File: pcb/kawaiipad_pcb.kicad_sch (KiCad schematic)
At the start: 21 parts, among them SW1 SW_Push_45deg, SW2 SW_Push_45deg, SW3 SW_Push_45deg, SW4 SW_Push_45deg, SW5 SW_Push_45deg, SW6 SW_Push_45deg, SW7 SW_Push_45deg, SW8 SW_Push_45deg, SW9 SW_Push_45deg, U1 XIAO-RP2040-DIP

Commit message: Update kawaiipad_pcb.kicad_sch
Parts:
- removed D1, D2: SK6812MINI, LED_SMD:LED_SK6812MINI_PLCC4_3.5x3.5mm_P1.75mm, symbol LED:SK6812MINI
- removed D10, D11: D, DiodeLibrary:Diode-Hybrid-Dual, symbol Device:D
- added D1, D2: D, symbol Device:D
- added D10, D11, D12, D13, D15, D16, D17, D18, D19: SK6812MINI, LED_SMD:LED_SK6812MINI_PLCC4_3.5x3.5mm_P1.75mm, symbol LED:SK6812MINI
- D3, D4, D5, D6, D7, D8, D9: footprint DiodeLibrary:Diode-Hybrid-Dual -> (none)
- SW1, SW2, SW3, SW4, SW5, SW6, SW7, SW8, SW9: footprint Button_Switch_Keyboard:SW_Cherry_MX_1.00u_PCB -> (none)
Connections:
- net +5V: now also D10.4 (VDD), D11.4 (VDD), D12.4 (VDD), D13.4 (VDD), D15.4 (VDD), D16.4 (VDD), D17.4 (VDD), D18.4 (VDD), D19.4 (VDD)
- net GND: now also D10.2 (VSS), D11.2 (VSS), D12.2 (VSS), D13.2 (VSS), D15.2 (VSS), D16.2 (VSS), D17.2 (VSS), D18.2 (VSS), D19.2 (VSS)
- net LED: now also D10.3 (DIN)
- net Row 0: now also D1.1 (K), D2.1 (K); no longer D4.1 (K), D5.1 (K)
- net Row 1: now also D4.1 (K), D5.1 (K); no longer D7.1 (K), D8.1 (K)
- net Row 2: now also D7.1 (K), D8.1 (K)
- net at SW8.2: now also D8.2 (A)
- net at D9.2 (A): now also SW9.2; no longer SW7.2
- net at SW6.2: now also D6.2 (A); no longer D8.2 (A)
- net at SW5.2: now also D5.2 (A); no longer D7.2 (A)
- net at SW4.2: now also D4.2 (A); no longer D6.2 (A)
- net at SW1.2: now also D1.2 (A); no longer D3.2 (A)
- net at SW3.2: now also D3.2 (A); no longer D5.2 (A)
- net at SW2.2: now also D2.2 (A); no longer D4.2 (A)
- new net: D10.1 (DOUT), D11.3 (DIN)
- new net: D11.1 (DOUT), D12.3 (DIN)
- new net: D16.1 (DOUT), D17.3 (DIN)
- new net: D15.1 (DOUT), D16.3 (DIN)
- new net: D7.2 (A), SW7.2
- new net: D12.1 (DOUT), D13.3 (DIN)
- new net: D13.1 (DOUT), D15.3 (DIN)
- new net: D18.1 (DOUT), D19.3 (DIN)
- new net: D17.1 (DOUT), D18.3 (DIN)
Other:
- note added: "RGB LEDs"
- note added: "RP2040 MCU"
- note added: "SWITCHES"
- title: (none) -> KawaiiPad
- moved on the sheet: U1

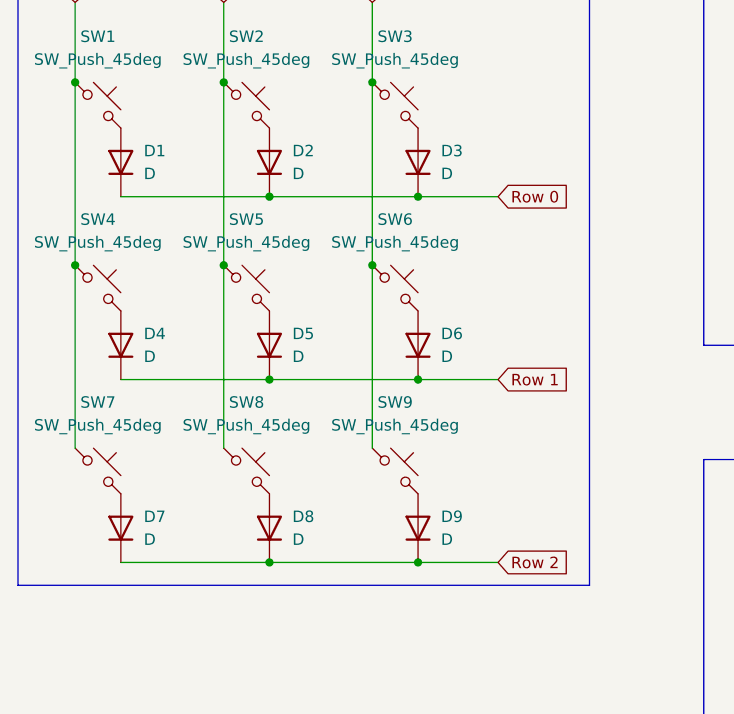
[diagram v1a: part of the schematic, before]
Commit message: Add Diode 1N418, remove accidental extra LEDs, assign footprints
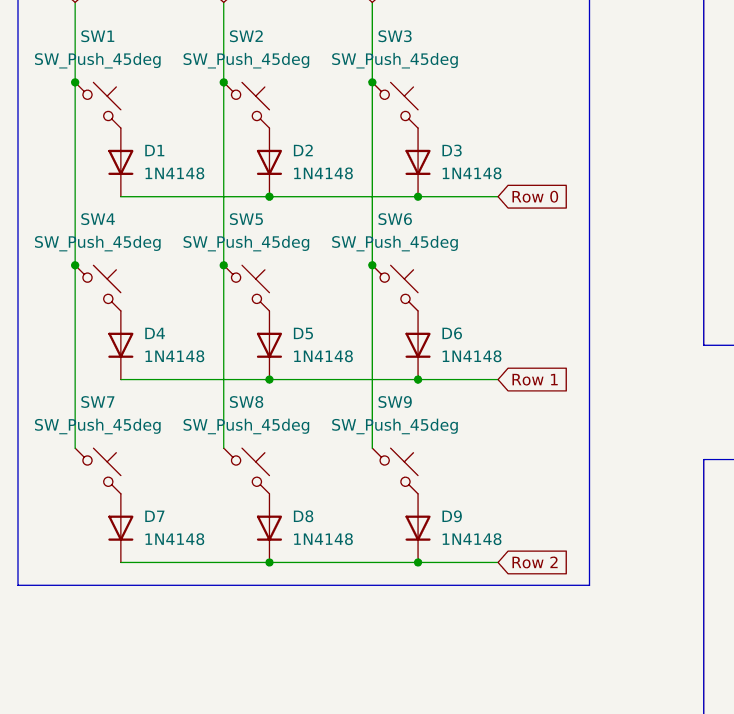
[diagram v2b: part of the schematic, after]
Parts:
- removed D1, D2, D3, D4, D5, D6, D7, D8, D9: D, symbol Device:D
- added D1, D2, D3, D4, D5, D6, D7, D8, D9: 1N4148, DiodeLibrary:DIODE-1N4148, symbol Diode:1N4148
- SW1, SW2, SW3, SW4, SW5, SW6, SW7, SW8, SW9: footprint (none) -> Button_Switch_Keyboard:SW_Cherry_MX_1.00u_PCB
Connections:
- net Row 0: now also D1.1 (K), D2.1 (K), D3.1 (K)
- net Row 1: now also D4.1 (K), D5.1 (K), D6.1 (K)
- net Row 2: now also D7.1 (K), D8.1 (K), D9.1 (K)
- net at SW9.2: now also D9.2 (A)
- net at SW4.2: now also D4.2 (A)
- net at SW5.2: now also D5.2 (A)
- net at SW1.2: now also D1.2 (A)
- net at SW7.2: now also D7.2 (A)
- net at SW6.2: now also D6.2 (A)
- net at SW2.2: now also D2.2 (A)
- net at SW8.2: now also D8.2 (A)
- net at SW3.2: now also D3.2 (A)

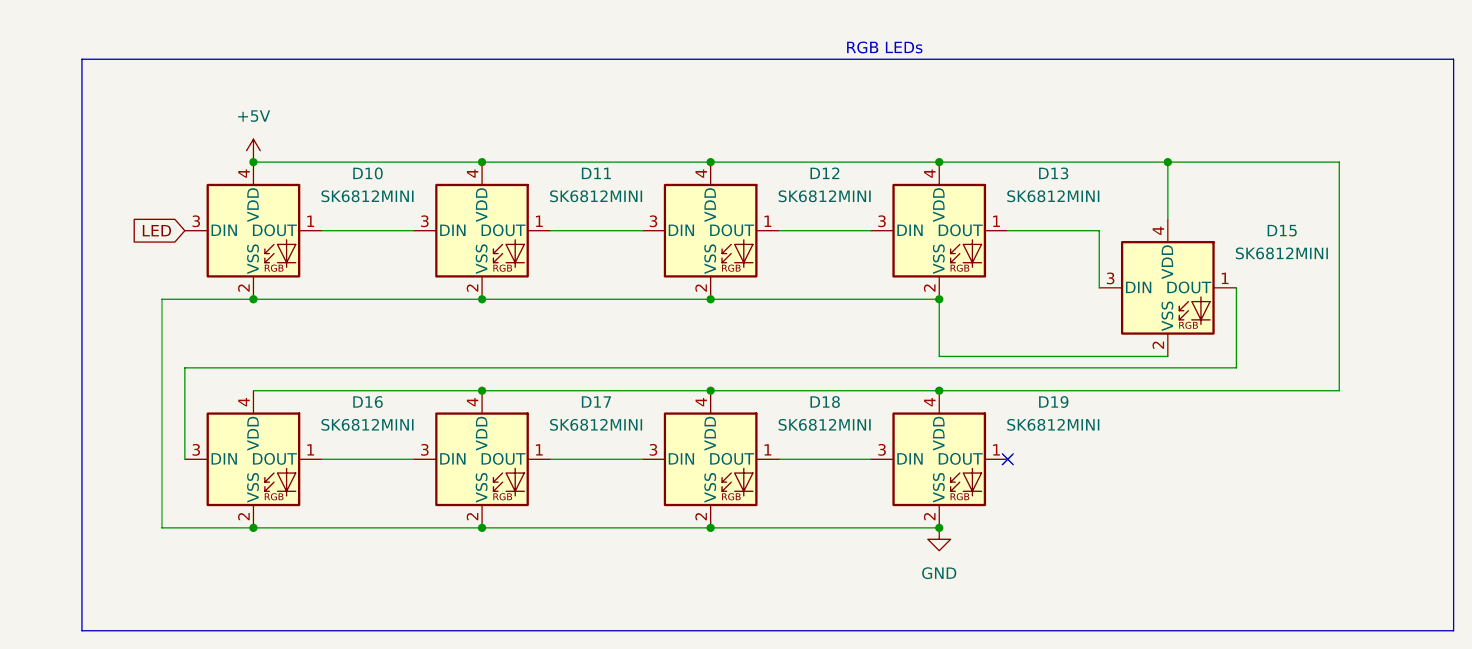
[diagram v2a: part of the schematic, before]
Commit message: clear pcb, fix schematic
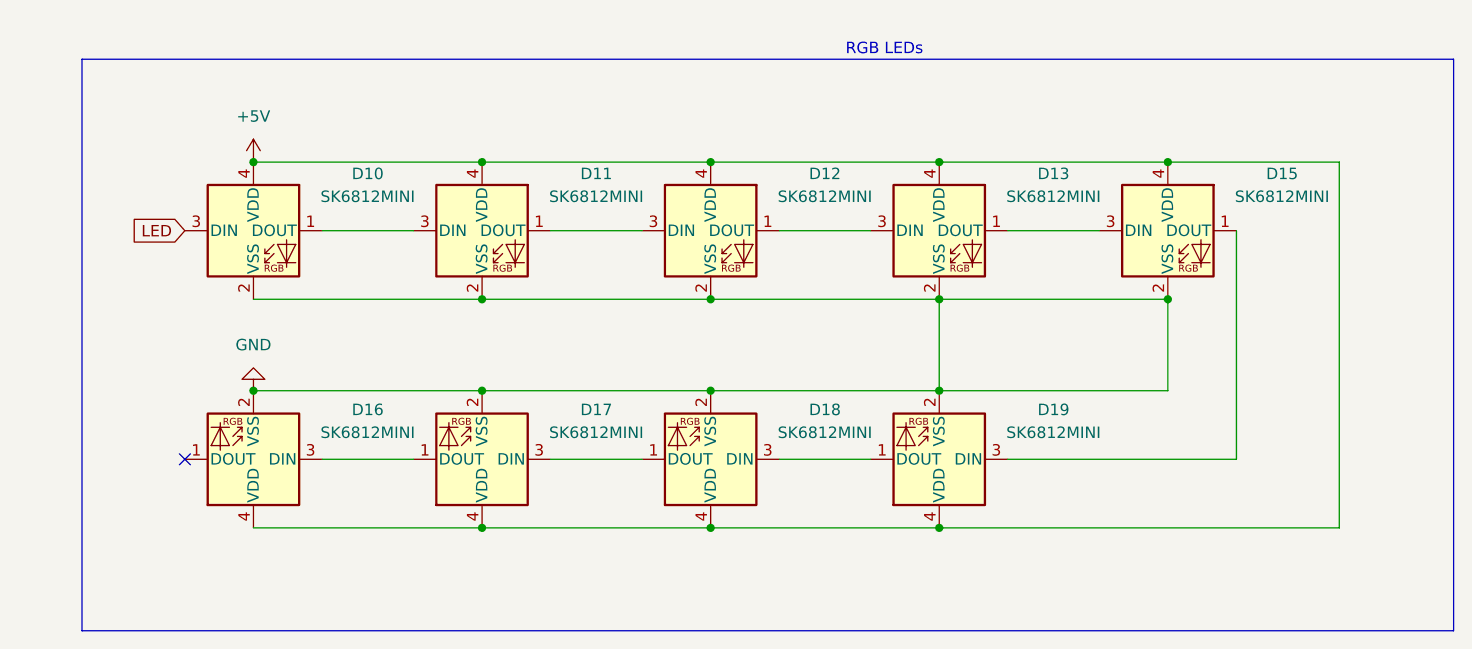
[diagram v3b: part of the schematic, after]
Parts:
- D1, D2, D3, D4, D5, D6, D7, D8, D9: footprint DiodeLibrary:DIODE-1N4148 -> DiodeLibrary:Diode-Hybrid-Dual
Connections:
- net at D16.1 (DOUT): no longer D17.3 (DIN)
- net at D16.3 (DIN): now also D17.1 (DOUT); no longer D15.1 (DOUT)
- net at D19.1 (DOUT): now also D18.3 (DIN)
- net at D19.3 (DIN): now also D15.1 (DOUT); no longer D18.1 (DOUT)
- new net: D17.3 (DIN), D18.1 (DOUT)
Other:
- moved on the sheet: D15, D16, D17, D18, D19

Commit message: finish PCB wiring
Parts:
- removed D19: SK6812MINI, LED_SMD:LED_SK6812MINI_PLCC4_3.5x3.5mm_P1.75mm, symbol LED:SK6812MINI
- added D14: SK6812MINI, LED_SMD:LED_SK6812MINI_PLCC4_3.5x3.5mm_P1.75mm, symbol LED:SK6812MINI
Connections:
- net +5V: now also D14.4 (VDD)
- net GND: now also D14.2 (VSS)
- net at D16.1 (DOUT): now also D17.3 (DIN)
- net at D17.1 (DOUT): now also D18.3 (DIN); no longer D16.3 (DIN)
- net at D15.3 (DIN): now also D14.1 (DOUT); no longer D13.1 (DOUT)
- net at D15.1 (DOUT): now also D16.3 (DIN)
- net at D18.1 (DOUT): no longer D17.3 (DIN)
- new net: D13.1 (DOUT), D14.3 (DIN)
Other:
- moved on the sheet: D1, D2, D3, D4, D5, D6, D7, D8, D9, SW1, SW2, SW3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
